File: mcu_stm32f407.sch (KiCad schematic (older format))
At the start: 23 parts, among them J1 Conn_01x05_Male, U1 STM32F407VGTx, Y1 8MHz

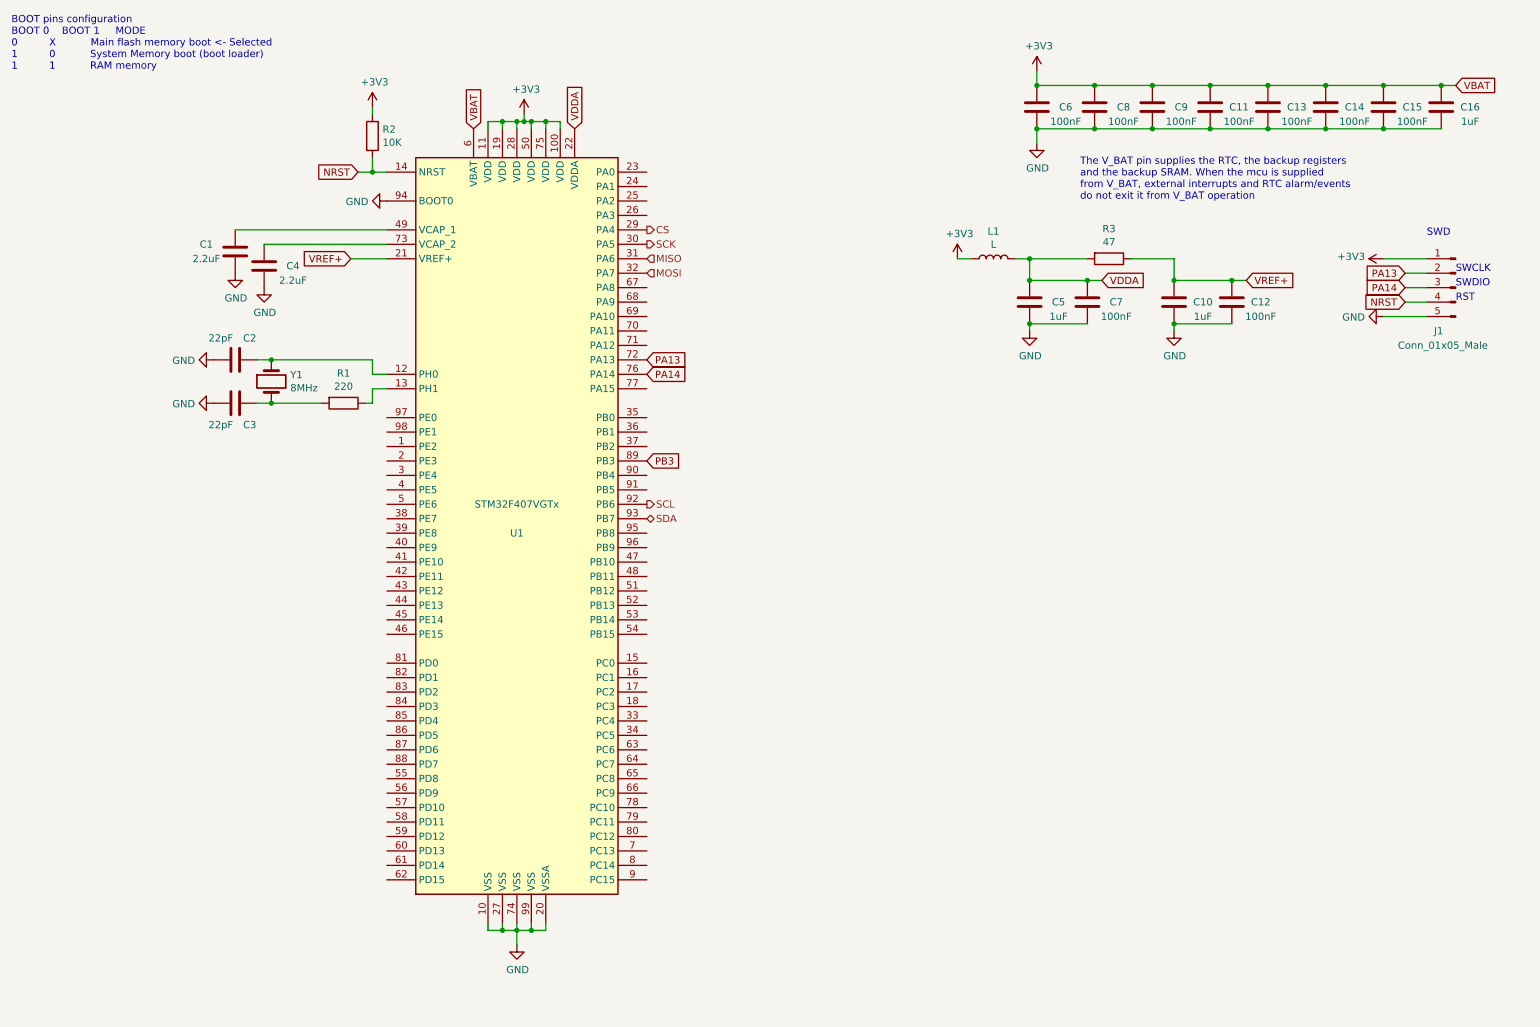
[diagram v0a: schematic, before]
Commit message: Changes only global labels to main page
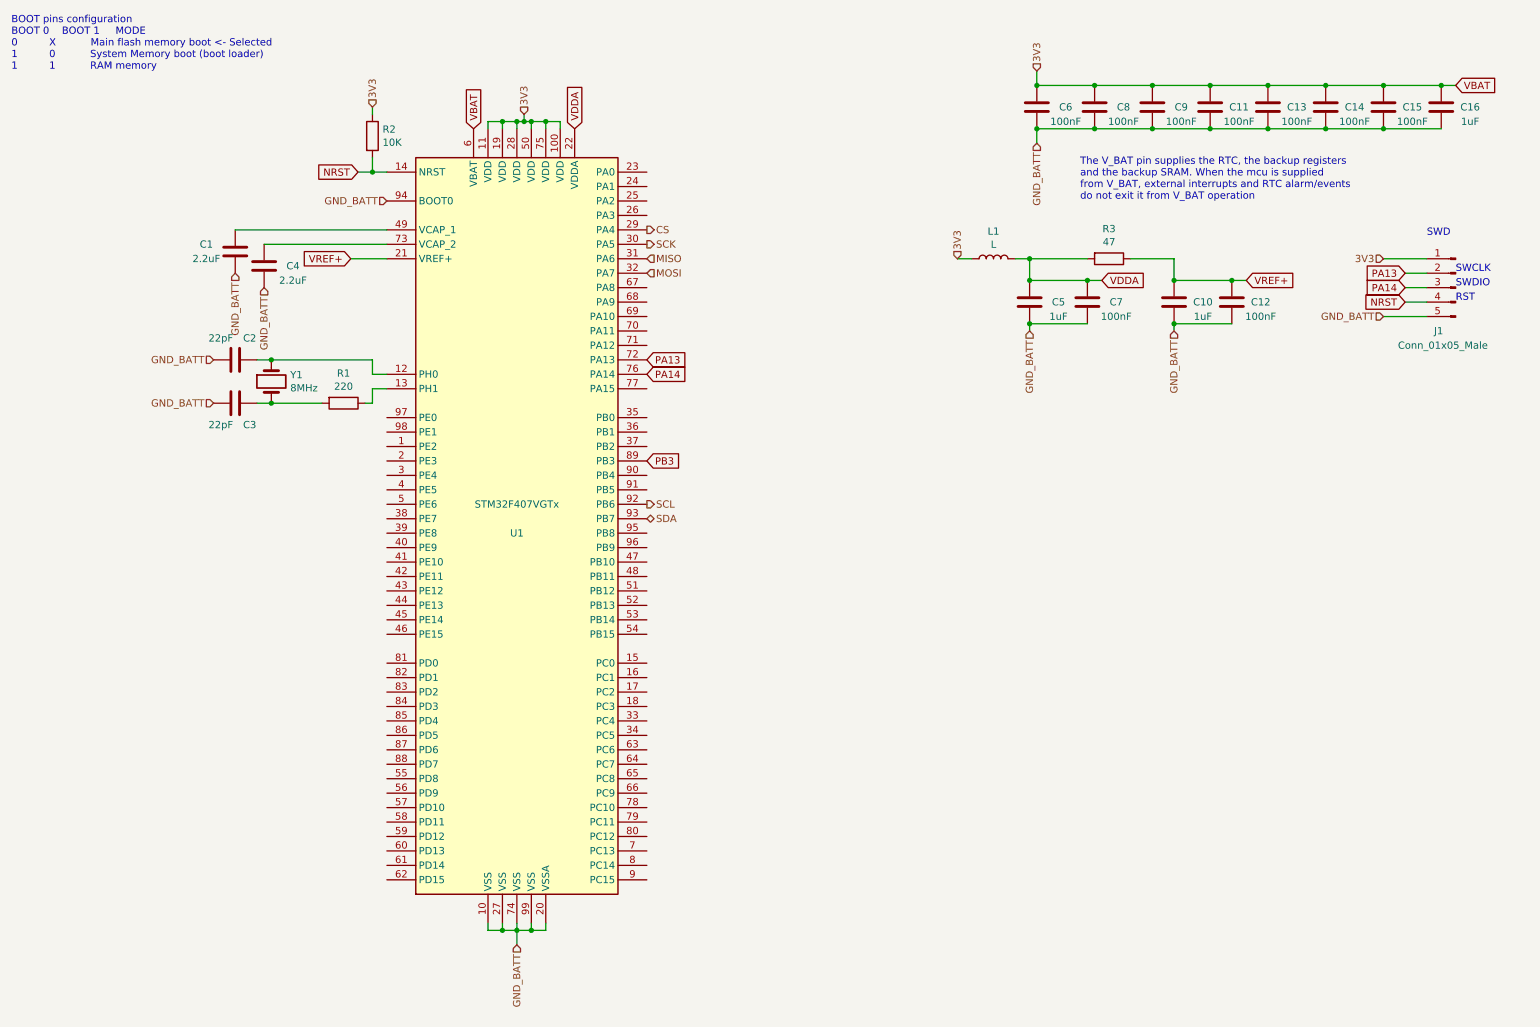
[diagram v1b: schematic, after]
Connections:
- net +3V3 renamed VBAT
- net GND renamed GND_BATT
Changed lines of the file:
@@
 $Descr A4 11693 8268
 encoding utf-8
-Sheet 3 7
+Sheet 7 7
 Title ""
 Date ""
@@
 Wire Wire Line
 	2350 2900 2250 2900
-$Comp
-L power:GND #PWR0101
-U 1 1 5FE55354
-P 1950 3200
-F 0 "#PWR0101" H 1950 2950 50  0001 C CNN
-F 1 "GND" V 1955 3072 50  0000 R CNN
-F 2 "" H 1950 3200 50  0001 C CNN
-F 3 "" H 1950 3200 50  0001 C CNN
-	1    1950 3200
-	0    1    1    0
-$EndComp
-$Comp
-L power:GND #PWR0102
-U 1 1 5FE55D5E
-P 1950 2900
-F 0 "#PWR0102" H 1950 2650 50  0001 C CNN
-F 1 "GND" V 1955 2772 50  0000 R CNN
-F 2 "" H 1950 2900 50  0001 C CNN
-F 3 "" H 1950 2900 50  0001 C CNN
-	1    1950 2900
-	0    1    1    0
-$EndComp
-$Comp
-L power:GND #PWR0103
-U 1 1 5FE58B7E
-P 4050 6950
-F 0 "#PWR0103" H 4050 6700 50  0001 C CNN
-F 1 "GND" H 4055 6777 50  0000 C CNN
-F 2 "" H 4050 6950 50  0001 C CNN
-F 3 "" H 4050 6950 50  0001 C CNN
-	1    4050 6950
-	1    0    0    -1
-$EndComp
 Wire Wire Line
 	3850 6800 3850 6850
@@
 	1    0    0    -1
 $EndComp
-$Comp
-L power:GND #PWR0104
-U 1 1 5FE60243
-P 2100 2300
-F 0 "#PWR0104" H 2100 2050 50  0001 C CNN
-F 1 "GND" H 2105 2127 50  0000 C CNN
-F 2 "" H 2100 2300 50  0001 C CNN
-F 3 "" H 2100 2300 50  0001 C CNN
-	1    2100 2300
-	1    0    0    -1
-$EndComp
-$Comp
-L power:GND #PWR0105
-U 1 1 5FE60676
-P 2300 2400
-F 0 "#PWR0105" H 2300 2150 50  0001 C CNN
-F 1 "GND" H 2305 2227 50  0000 C CNN
-F 2 "" H 2300 2400 50  0001 C CNN
-F 3 "" H 2300 2400 50  0001 C CNN
-	1    2300 2400
-	1    0    0    -1
-$EndComp
 Text GLabel 2900 2200 0    50   Input ~ 0
 VREF+
@@
 Connection ~ 4050 1250
 Wire Wire Line
-	4050 1250 4100 1250
-Wire Wire Line
 	4150 1300 4150 1250
 Connection ~ 4150 1250
@@
 Wire Wire Line
 	4250 1250 4350 1250
-Wire Wire Line
-	4100 1200 4100 1250
-Connection ~ 4100 1250
-Wire Wire Line
-	4100 1250 4150 1250
 $Comp
 L Device:R R1
@@
 Wire Wire Line
 	8450 1000 8850 1000
-$Comp
-L power:GND #PWR0106
-U 1 1 5FE886F8
-P 7650 1400
-F 0 "#PWR0106" H 7650 1150 50  0001 C CNN
-F 1 "GND" H 7655 1227 50  0000 C CNN
-F 2 "" H 7650 1400 50  0001 C CNN
-F 3 "" H 7650 1400 50  0001 C CNN
-	1    7650 1400
-	1    0    0    -1
-$EndComp
 Wire Wire Line
 	7650 1300 7650 1400
@@
 Wire Wire Line
 	7600 2350 8000 2350
-$Comp
-L power:GND #PWR0107
-U 1 1 5FEBA6FA
-P 7600 2700
-F 0 "#PWR0107" H 7600 2450 50  0001 C CNN
-F 1 "GND" H 7605 2527 50  0000 C CNN
-F 2 "" H 7600 2700 50  0001 C CNN
-F 3 "" H 7600 2700 50  0001 C CNN
-	1    7600 2700
-	1    0    0    -1
-$EndComp
 Wire Wire Line
 	7600 2650 8000 2650
@@
 Wire Wire Line
 	8600 2350 9000 2350
-$Comp
-L power:GND #PWR0108
-U 1 1 5FEC05DE
-P 8600 2700
-F 0 "#PWR0108" H 8600 2450 50  0001 C CNN
-F 1 "GND" H 8605 2527 50  0000 C CNN
-F 2 "" H 8600 2700 50  0001 C CNN
-F 3 "" H 8600 2700 50  0001 C CNN
-	1    8600 2700
-	1    0    0    -1
-$EndComp
 Wire Wire Line
 	8600 2650 9000 2650
@@
 	9000 2350 9100 2350
 Connection ~ 9000 2350
-$Comp
-L power:GND #PWR0109
-U 1 1 5FEC5C85
-P 3150 1800
-F 0 "#PWR0109" H 3150 1550 50  0001 C CNN
-F 1 "GND" V 3155 1672 50  0000 R CNN
-F 2 "" H 3150 1800 50  0001 C CNN
-F 3 "" H 3150 1800 50  0001 C CNN
-	1    3150 1800
-	0    1    1    0
-$EndComp
 Text Notes 550  900  0    50   ~ 0
 BOOT pins configuration\nBOOT 0    BOOT 1     MODE\n0          X           Main flash memory boot <- Selected\n1          0           System Memory boot (boot loader)\n1          1           RAM memory
@@
 Wire Wire Line
 	10200 2500 10350 2500
-$Comp
-L power:GND #PWR0110
-U 1 1 5FF09E8C
-P 10050 2600
-F 0 "#PWR0110" H 10050 2350 50  0001 C CNN
-F 1 "GND" V 10055 2472 50  0000 R CNN
-F 2 "" H 10050 2600 50  0001 C CNN
-F 3 "" H 10050 2600 50  0001 C CNN
-	1    10050 2600
-	0    1    1    0
-$EndComp
 Wire Wire Line
 	10050 2600 10350 2600
@@
 Text Notes 10550 2500 0    50   ~ 0
 RST
-$Comp
-L power:+3V3 #PWR0111
-U 1 1 5FF5411F
-P 4100 1200
-F 0 "#PWR0111" H 4100 1050 50  0001 C CNN
-F 1 "+3V3" H 4115 1373 50  0000 C CNN
-F 2 "" H 4100 1200 50  0001 C CNN
-F 3 "" H 4100 1200 50  0001 C CNN
-	1    4100 1200
-	1    0    0    -1
-$EndComp
-$Comp
-L power:+3V3 #PWR0112
-U 1 1 5FF546A9
-P 3050 1150
-F 0 "#PWR0112" H 3050 1000 50  0001 C CNN
-F 1 "+3V3" H 3065 1323 50  0000 C CNN
-F 2 "" H 3050 1150 50  0001 C CNN
-F 3 "" H 3050 1150 50  0001 C CNN
-	1    3050 1150
-	1    0    0    -1
-$EndComp
-$Comp
-L power:+3V3 #PWR0113
-U 1 1 5FF54A00
-P 7650 900
-F 0 "#PWR0113" H 7650 750 50  0001 C CNN
-F 1 "+3V3" H 7665 1073 50  0000 C CNN
-F 2 "" H 7650 900 50  0001 C CNN
-F 3 "" H 7650 900 50  0001 C CNN
-	1    7650 900
-	1    0    0    -1
-$EndComp
-$Comp
-L power:+3V3 #PWR0114
-U 1 1 5FF54EB4
-P 7100 2200
-F 0 "#PWR0114" H 7100 2050 50  0001 C CNN
-F 1 "+3V3" H 7115 2373 50  0000 C CNN
-F 2 "" H 7100 2200 50  0001 C CNN
-F 3 "" H 7100 2200 50  0001 C CNN
-	1    7100 2200
-	1    0    0    -1
-$EndComp
-$Comp
-L power:+3V3 #PWR0115
-U 1 1 5FF552E6
-P 10050 2200
-F 0 "#PWR0115" H 10050 2050 50  0001 C CNN
-F 1 "+3V3" V 10065 2328 50  0000 L CNN
-F 2 "" H 10050 2200 50  0001 C CNN
-F 3 "" H 10050 2200 50  0001 C CNN
-	1    10050 2200
-	0    -1   -1   0
-$EndComp
 Text HLabel 4950 4000 2    50   BiDi ~ 0
 SDA
@@
 Text HLabel 4950 2000 2    50   Output ~ 0
 CS
+Text HLabel 4100 1200 1    50   Input ~ 0
+3V3
+Wire Wire Line
+	4050 1250 4100 1250
+Wire Wire Line
+	4100 1200 4100 1250
+Connection ~ 4100 1250
+Wire Wire Line
+	4100 1250 4150 1250
+Text HLabel 4050 6950 3    50   Input ~ 0
+GND_BATT
+Text HLabel 7600 2700 3    50   Input ~ 0
+GND_BATT
+Text HLabel 8600 2700 3    50   Input ~ 0
+GND_BATT
+Text HLabel 10050 2600 0    50   Input ~ 0
+GND_BATT
+Text HLabel 10050 2200 0    50   Input ~ 0
+3V3
+Text HLabel 7650 900  1    50   Input ~ 0
+3V3
+Text HLabel 7100 2200 1    50   Input ~ 0
+3V3
+Text HLabel 3050 1150 1    50   Input ~ 0
+3V3
+Text HLabel 3150 1800 0    50   Input ~ 0
+GND_BATT
+Text HLabel 1950 2900 0    50   Input ~ 0
+GND_BATT
+Text HLabel 1950 3200 0    50   Input ~ 0
+GND_BATT
+Text HLabel 2100 2300 3    50   Input ~ 0
+GND_BATT
+Text HLabel 2300 2400 3    50   Input ~ 0
+GND_BATT
+Text HLabel 7650 1400 3    50   Input ~ 0
+GND_BATT
 $EndSCHEMATC

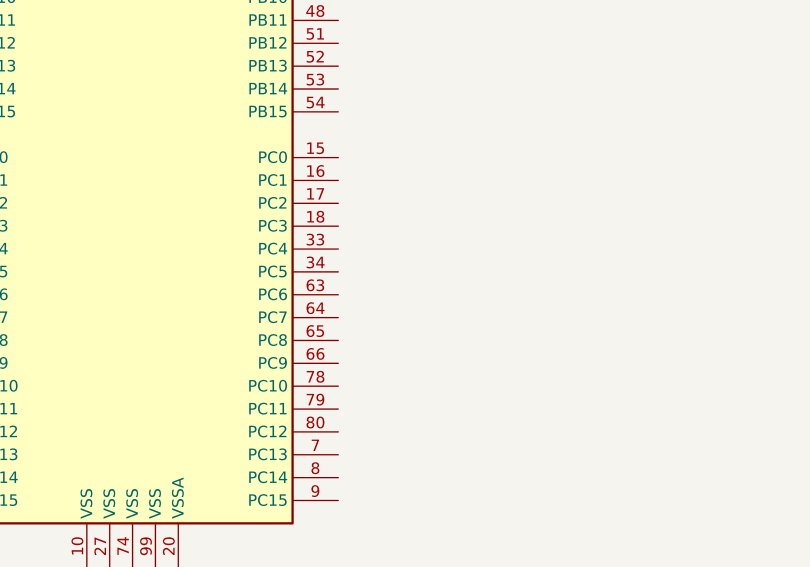
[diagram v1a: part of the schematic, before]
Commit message: Adds aux pins for bq76
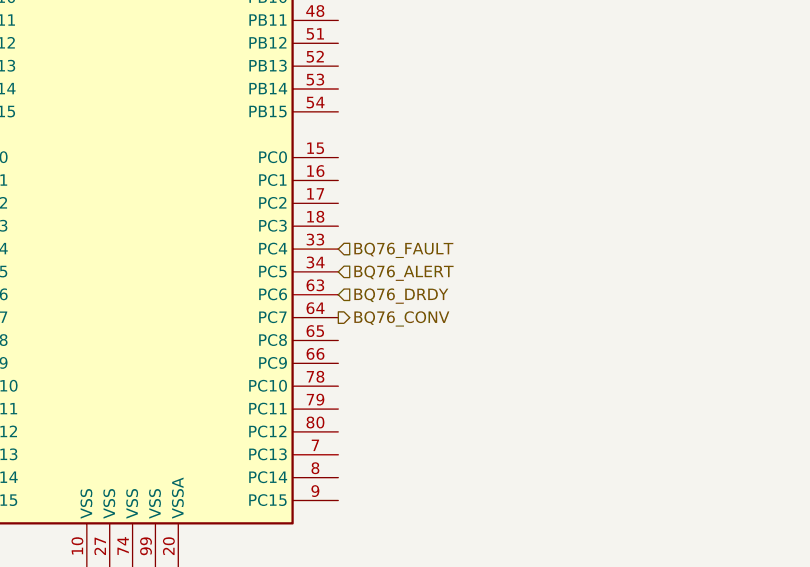
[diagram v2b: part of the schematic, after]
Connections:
- net BQ76_FAULT: now reaches U1.33 (PC4)
- net BQ76_ALERT: now reaches U1.34 (PC5)
- net BQ76_DRDY: now reaches U1.63 (PC6)
- net BQ76_CONV: now reaches U1.64 (PC7)
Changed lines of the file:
@@
 Text HLabel 7650 1400 3    50   Input ~ 0
 GND_BATT
+Text HLabel 4950 5400 2    50   Input ~ 0
+BQ76_FAULT
+Text HLabel 4950 5500 2    50   Input ~ 0
+BQ76_ALERT
+Text HLabel 4950 5600 2    50   Input ~ 0
+BQ76_DRDY
+Text HLabel 4950 5700 2    50   Output ~ 0
+BQ76_CONV
 $EndSCHEMATC

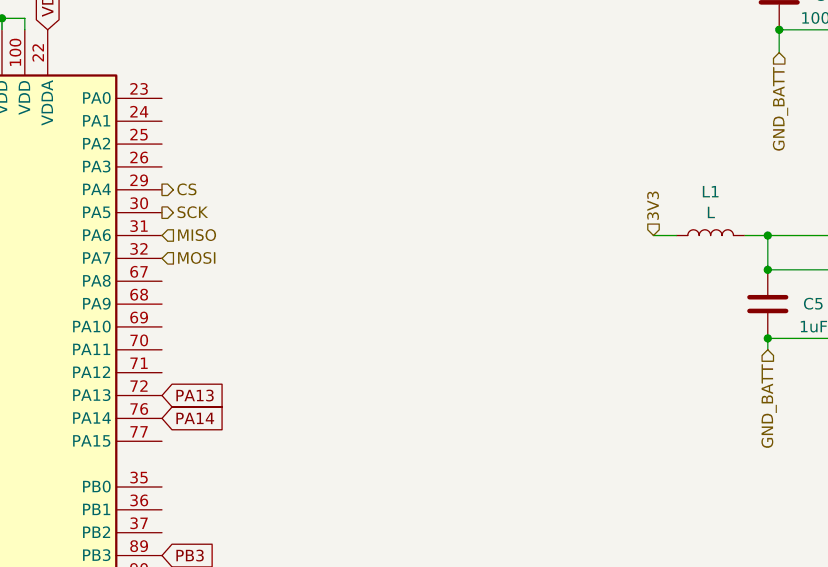
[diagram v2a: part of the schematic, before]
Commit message: Adds Can Pins
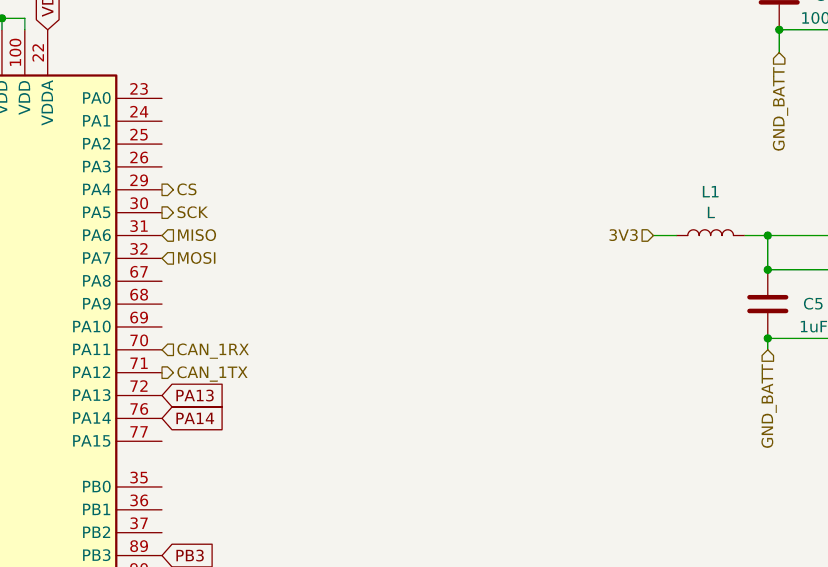
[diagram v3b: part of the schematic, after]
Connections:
- net CAN_1RX: now reaches U1.70 (PA11)
- net CAN_1TX: now reaches U1.71 (PA12)
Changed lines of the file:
@@
 Text HLabel 7650 900  1    50   Input ~ 0
 3V3
-Text HLabel 7100 2200 1    50   Input ~ 0
+Text HLabel 7100 2200 0    50   Input ~ 0
 3V3
 Text HLabel 3050 1150 1    50   Input ~ 0
@@
 Text HLabel 4950 5700 2    50   Output ~ 0
 BQ76_CONV
+Text HLabel 4950 2700 2    50   Input ~ 0
+CAN_1RX
+Text HLabel 4950 2800 2    50   Output ~ 0
+CAN_1TX
 $EndSCHEMATC
